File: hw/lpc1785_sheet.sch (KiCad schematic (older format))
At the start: 26 parts, among them J2 ARM_JTAG_SWD_HEADER_10_PINSMD, J3 HEADER_USART_2_SMD, U4 LPC1785FBD208_551QFP50, X1 XTAL_7A-20.000MAAJ-T

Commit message: PCB was too big for itead, reduced size and ordered one
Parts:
- J3: footprint usevolt:usevolt-HEADER_4_2_SMD -> usevolt:HEADER_4_2_SMD
- U4: footprint usevolt:usevolt-QFP208 -> usevolt:QFP208
- X1: footprint usevolt:usevolt-XTAL_7A-20.000MAJ -> usevolt:XTAL_7A-20.000MAJ
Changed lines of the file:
@@
 F 0 "U4" H 7150 7354 45  0000 C CNN
 F 1 "LPC1785FBD208_551QFP50" H 7150 7270 45  0000 C CNN
-F 2 "usevolt:usevolt-QFP208" H 6730 5550 20  0001 C CNN
+F 2 "usevolt:QFP208" H 6730 5550 20  0001 C CNN
 F 3 "http://www.nxp.com/documents/data_sheet/LPC178X_7X.pdf" H 6871 7282 60  0001 C CNN
 F 4 "568-7573-ND" H 7271 7682 60  0001 C CNN "1st Source Part Number"
@@
 F 0 "U4" H 14150 6804 45  0000 C CNN
 F 1 "LPC1785FBD208_551QFP50" H 14150 6720 45  0000 C CNN
-F 2 "usevolt:usevolt-QFP208" H 13030 5200 20  0001 C CNN
+F 2 "usevolt:QFP208" H 13030 5200 20  0001 C CNN
 F 3 "http://www.nxp.com/documents/data_sheet/LPC178X_7X.pdf" H 13171 6932 60  0001 C CNN
 F 4 "568-7573-ND" H 13571 7332 60  0001 C CNN "1st Source Part Number"
@@
 F 0 "U4" H 7050 12154 45  0000 C CNN
 F 1 "LPC1785FBD208_551QFP50" H 7050 12070 45  0000 C CNN
-F 2 "usevolt:usevolt-QFP208" H 5980 10650 20  0001 C CNN
+F 2 "usevolt:QFP208" H 5980 10650 20  0001 C CNN
 F 3 "http://www.nxp.com/documents/data_sheet/LPC178X_7X.pdf" H 6121 12382 60  0001 C CNN
 F 4 "568-7573-ND" H 6521 12782 60  0001 C CNN "1st Source Part Number"
@@
 F 0 "U4" H 13800 12554 45  0000 C CNN
 F 1 "LPC1785FBD208_551QFP50" H 13800 12470 45  0000 C CNN
-F 2 "usevolt:usevolt-QFP208" H 12830 10750 20  0001 C CNN
+F 2 "usevolt:QFP208" H 12830 10750 20  0001 C CNN
 F 3 "http://www.nxp.com/documents/data_sheet/LPC178X_7X.pdf" H 12971 12482 60  0001 C CNN
 F 4 "568-7573-ND" H 13371 12882 60  0001 C CNN "1st Source Part Number"
@@
 F 0 "X1" V 11508 9498 45  0000 L CNN
 F 1 "XTAL_7A-20.000MAAJ-T" V 11592 9498 45  0000 L CNN
-F 2 "usevolt:usevolt-XTAL_7A-20.000MAJ" H 11630 9550 20  0001 C CNN
+F 2 "usevolt:XTAL_7A-20.000MAJ" H 11630 9550 20  0001 C CNN
 F 3 "http://www.farnell.com/datasheets/1041607.pdf?_ga=1.225290842.1948984246.1460023966" H 11620 9420 60  0001 C CNN
 F 4 "1841950" H 12020 9820 60  0001 C CNN "1st Source Part Number"
@@
 F 0 "J3" H 19077 10292 45  0000 L CNN
 F 1 "HEADER_USART_2_SMD" H 19077 10208 45  0000 L CNN
-F 2 "usevolt:usevolt-HEADER_4_2_SMD" H 18680 10550 20  0001 C CNN
+F 2 "usevolt:HEADER_4_2_SMD" H 18680 10550 20  0001 C CNN
 F 3 "" H 18650 10400 60  0000 C CNN
 	1    18650 10400
@@
 $Bitmap
 Pos 22650 15250
-Scale 1,000000
+Scale 1.000000
 Data
 89 50 4E 47 0D 0A 1A 0A 00 00 00 0D 49 48 44 52 00 00 00 7B 00 00 00 49 08 02 00 00 00 92 17 CE

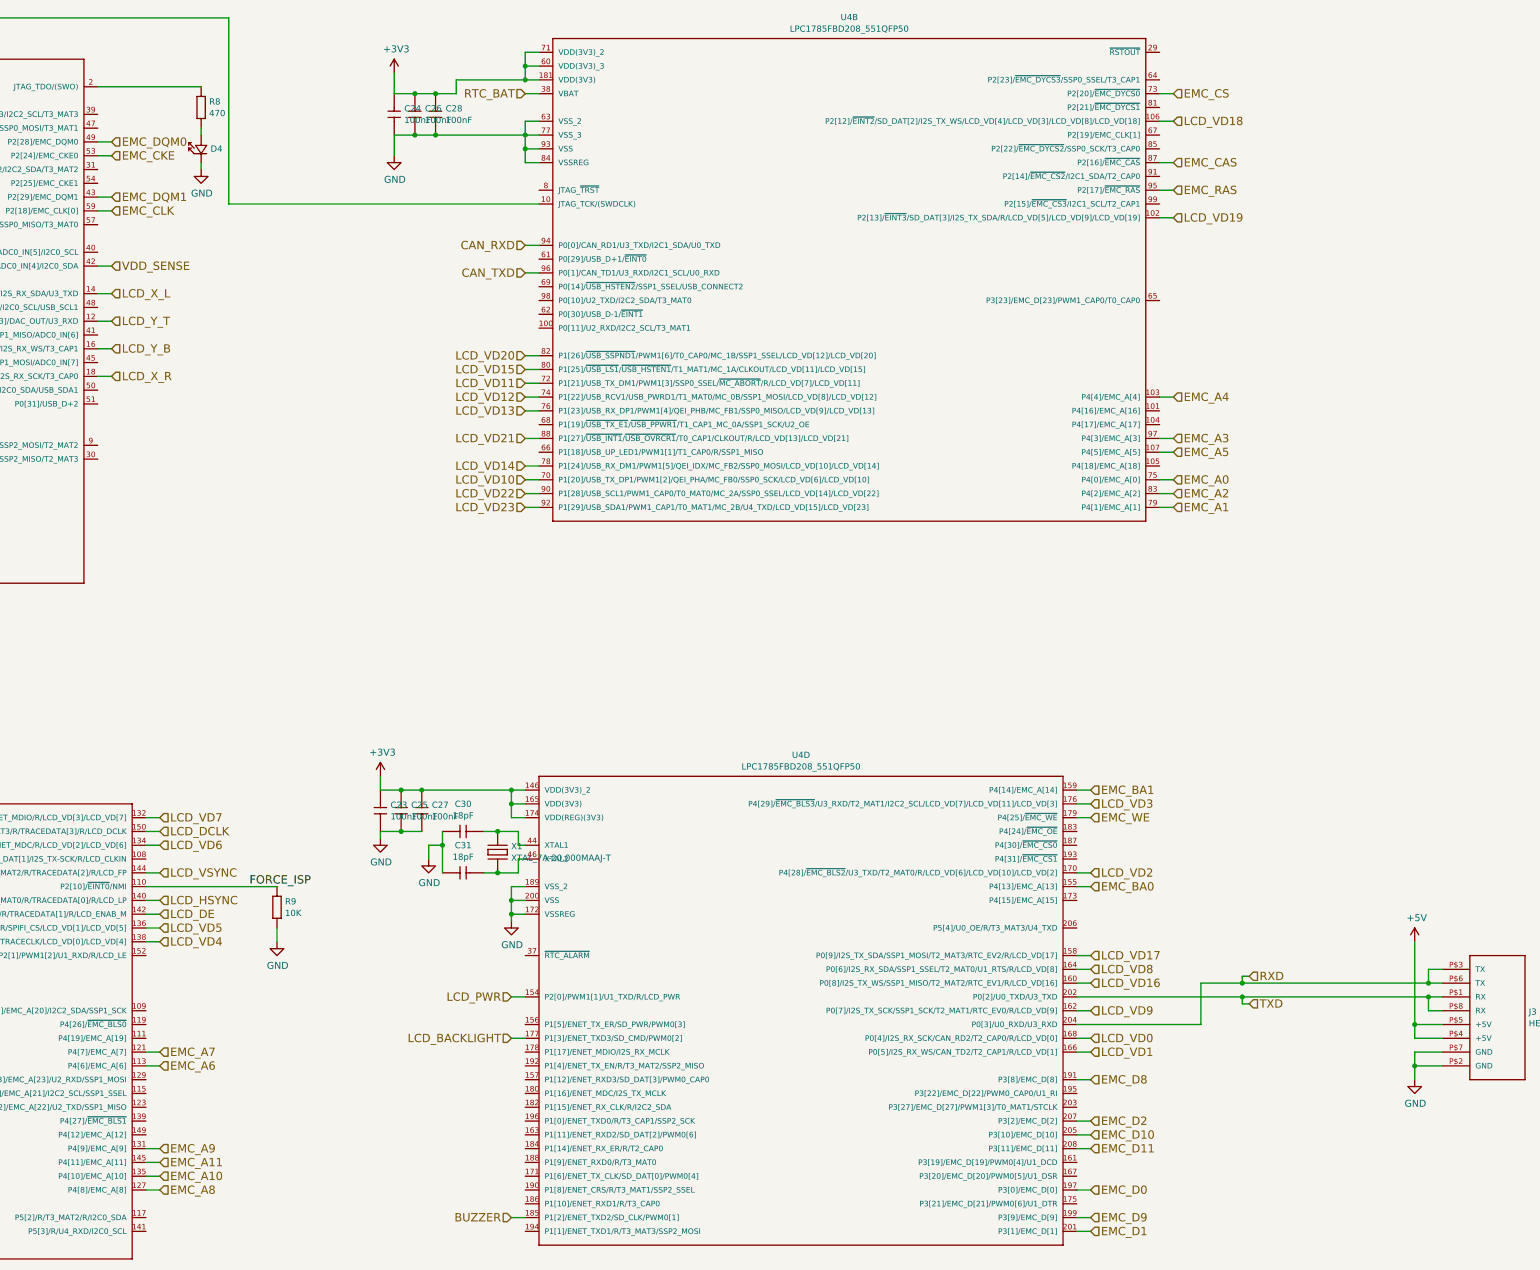
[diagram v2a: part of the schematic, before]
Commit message: HW revision 3 ordered from itead
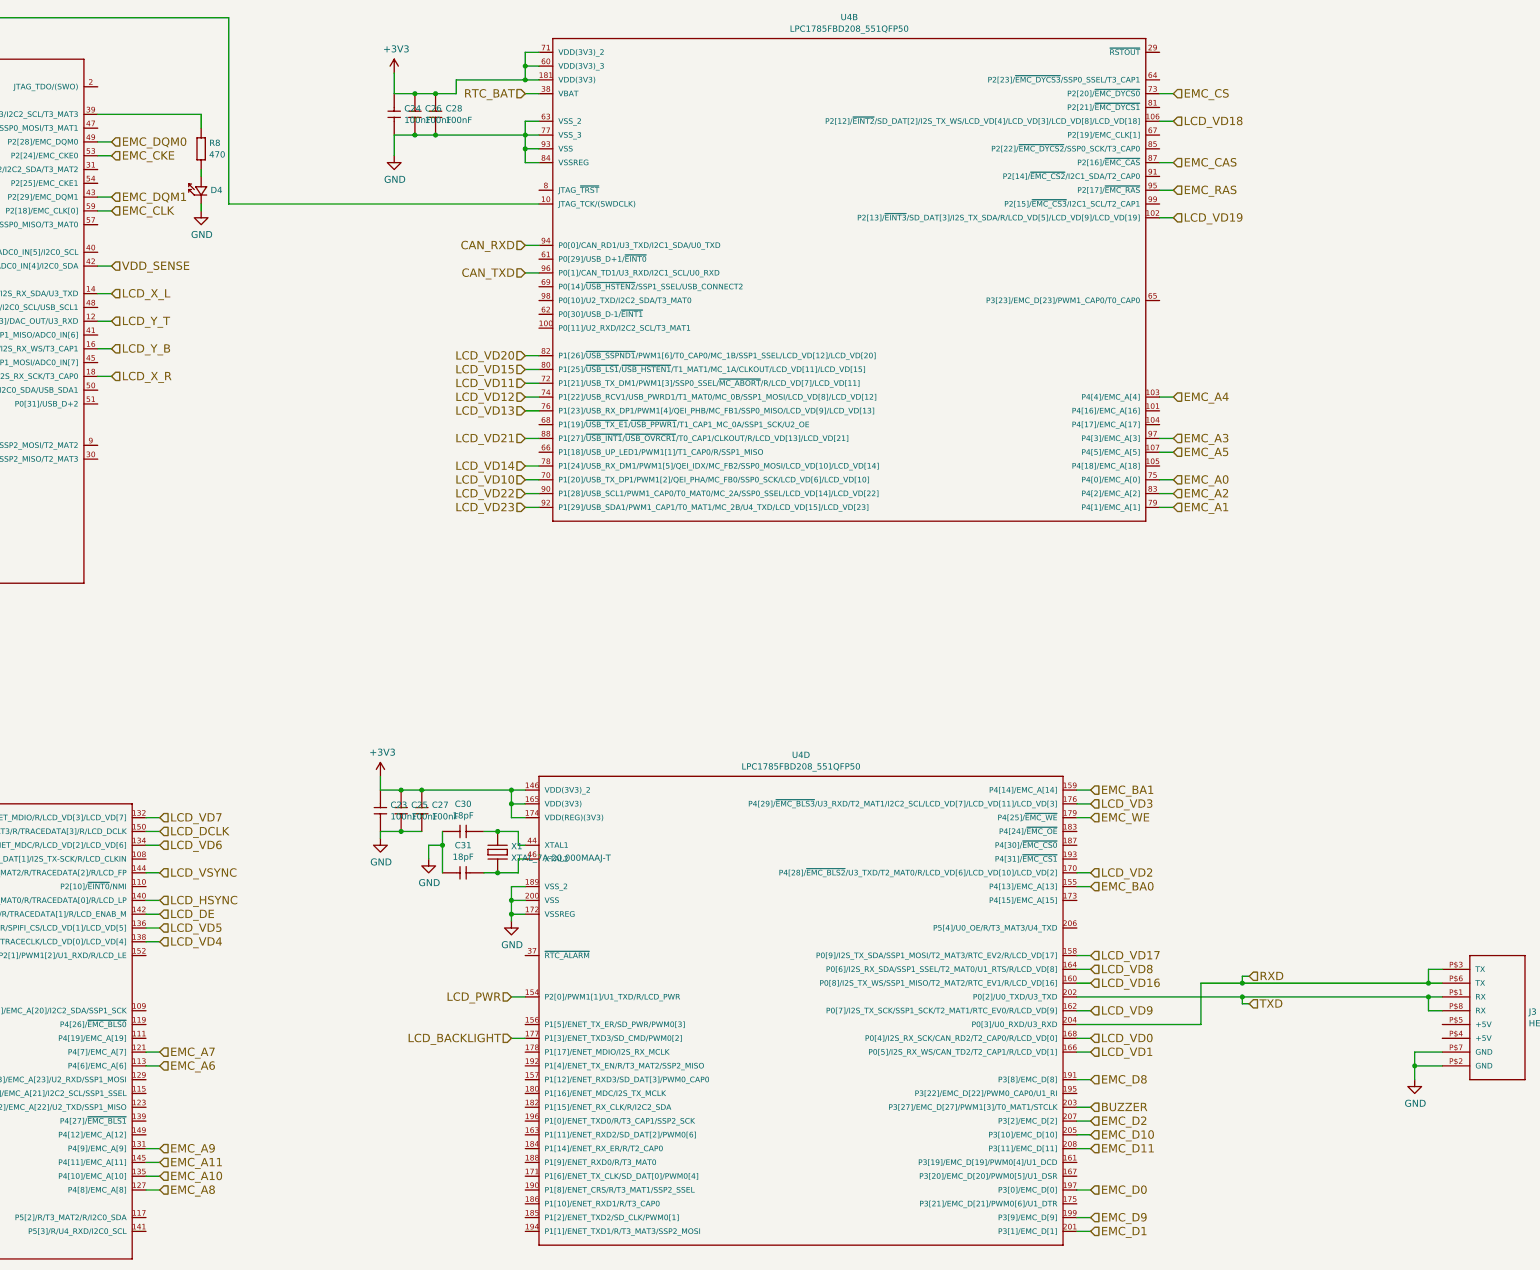
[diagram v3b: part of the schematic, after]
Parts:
- removed R9: 10K, multicomp:Multicomp-RESC1608X60N, symbol 10K
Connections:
- net BUZZER: now also U4.203 (P3[27]/EMC_D[27]/PWM1[3]/T0_MAT1/STCLK); no longer U4.185 (P1[2]/ENET_TXD2/SD_CLK/PWM0[1])
- net at U4.2 (JTAG_TDO/(SWO)): no longer R8.2 (R2)
- net at U4.39 (P2[31]/EMC_DQM3/I2C2_SCL/T3_MAT3): now also R8.2 (R2)
- net +5V: no longer names the net of J3.P$4 (+5V)
- net +5V: no longer J3.P$5 (+5V)
- net FORCE_ISP: no longer names the net of U4.110 (P2[10]/~EINT0~/NMI)
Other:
- moved on the sheet: D4, R8
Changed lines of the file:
@@
 L 470 R8
 U 1 1 57B5BC06
-P 9450 3900
-F 0 "R8" V 9458 3958 45  0000 L CNN
-F 1 "470" V 9542 3958 45  0000 L CNN
-F 2 "multicomp:Multicomp-RESC1608X60N" H 9480 4050 20  0001 C CNN
-F 3 "" H 9419 3939 60  0001 C CNN
-F 4 "9331239" H 9819 4339 60  0001 C CNN "1st Source Part Number"
-F 5 "Farnell" H 9719 4239 60  0001 C CNN "1st Source"
-F 6 "MC0063W06031470R" H 9619 4139 60  0001 C CNN "Manufacturer Part Number"
-F 7 "MULTICOMP" H 9519 4039 60  0001 C CNN "Manufacturer"
-	1    9450 3900
-	0    1    1    0
-$EndComp
-Wire Wire Line
-	9450 4150 9450 4100
-Wire Wire Line
-	9450 3800 8700 3800
+P 9450 4200
+F 0 "R8" V 9458 4258 45  0000 L CNN
+F 1 "470" V 9542 4258 45  0000 L CNN
+F 2 "multicomp:Multicomp-RESC1608X60N" H 9480 4350 20  0001 C CNN
+F 3 "" H 9419 4239 60  0001 C CNN
+F 4 "9331239" H 9819 4639 60  0001 C CNN "1st Source Part Number"
+F 5 "Farnell" H 9719 4539 60  0001 C CNN "1st Source"
+F 6 "MC0063W06031470R" H 9619 4439 60  0001 C CNN "Manufacturer Part Number"
+F 7 "MULTICOMP" H 9519 4339 60  0001 C CNN "Manufacturer"
+	1    9450 4200
+	0    1    1    0
+$EndComp
+Wire Wire Line
+	9450 4450 9450 4400
 $Comp
 L WL-SMCW-150060BS75000-B D4
 U 1 1 57B5C226
-P 9450 4250
-F 0 "D4" V 9450 4182 45  0000 R CNN
-F 1 "WL-SMCW-150060BS75000-B" H 9650 4350 45  0001 L BNN
-F 2 "wurth_LEDS:Wuerth_Elektronik_LEDs_rev15b-0603" H 9480 4400 20  0001 C CNN
-F 3 "http://www.farnell.com/datasheets/1911343.pdf?_ga=1.259491274.1948984246.1460023966" H 9250 4450 60  0001 C CNN
-F 4 "150060BS75000" H 9659 4453 60  0001 C CNN "Manufacturer Part Number"
-F 5 "2322069" H 9859 4653 60  0001 C CNN "1st Source Part Number"
-F 6 "Farnell" H 9759 4553 60  0001 C CNN "1st Source"
-F 7 "WURTH ELEKTRONIK" H 9559 4353 60  0001 C CNN "Manufacturer"
-	1    9450 4250
+P 9450 4550
+F 0 "D4" V 9450 4482 45  0000 R CNN
+F 1 "WL-SMCW-150060BS75000-B" H 9650 4650 45  0001 L BNN
+F 2 "wurth_LEDS:Wuerth_Elektronik_LEDs_rev15b-0603" H 9480 4700 20  0001 C CNN
+F 3 "http://www.farnell.com/datasheets/1911343.pdf?_ga=1.259491274.1948984246.1460023966" H 9250 4750 60  0001 C CNN
+F 4 "150060BS75000" H 9659 4753 60  0001 C CNN "Manufacturer Part Number"
+F 5 "2322069" H 9859 4953 60  0001 C CNN "1st Source Part Number"
+F 6 "Farnell" H 9759 4853 60  0001 C CNN "1st Source"
+F 7 "WURTH ELEKTRONIK" H 9559 4653 60  0001 C CNN "Manufacturer"
+	1    9450 4550
 	0    -1   -1   0
 $EndComp
@@
 L GND #PWR032
 U 1 1 57B5C2C2
-P 9450 4400
-F 0 "#PWR032" H 9450 4150 50  0001 C CNN
-F 1 "GND" H 9455 4227 50  0000 C CNN
-F 2 "" H 9450 4400 50  0000 C CNN
-F 3 "" H 9450 4400 50  0000 C CNN
-	1    9450 4400
-	1    0    0    -1
-$EndComp
-Wire Wire Line
-	9450 4400 9450 4350
+P 9450 4700
+F 0 "#PWR032" H 9450 4450 50  0001 C CNN
+F 1 "GND" H 9455 4527 50  0000 C CNN
+F 2 "" H 9450 4700 50  0000 C CNN
+F 3 "" H 9450 4700 50  0000 C CNN
+	1    9450 4700
+	1    0    0    -1
+$EndComp
+Wire Wire Line
+	9450 4700 9450 4650
 Text HLabel 8800 4200 2    60   Input ~ 0
 EMC_DQM0
@@
 Wire Wire Line
 	9150 9800 9050 9800
-$Comp
-L 10K R9
-U 1 1 57B6C633
-P 10000 9700
-F 0 "R9" V 10008 9758 45  0000 L CNN
-F 1 "10K" V 10092 9758 45  0000 L CNN
-F 2 "multicomp:Multicomp-RESC1608X60N" H 10030 9850 20  0001 C CNN
-F 3 "http://www.farnell.com/datasheets/1788326.pdf?_ga=1.214208087.1948984246.1460023966" H 9969 9739 60  0001 C CNN
-F 4 "9330399" H 10369 10139 60  0001 C CNN "1st Source Part Number"
-F 5 "Farnell" H 10269 10039 60  0001 C CNN "1st Source"
-F 6 "MC0063W0603110K" H 10169 9939 60  0001 C CNN "Manufacturer Part Number"
-F 7 "MULTICOMP" H 10069 9839 60  0001 C CNN "Manufacturer"
-	1    10000 9700
-	0    1    1    0
-$EndComp
-Wire Wire Line
-	10000 9600 9050 9600
-$Comp
-L GND #PWR033
-U 1 1 57B6C7FA
-P 10000 10000
-F 0 "#PWR033" H 10000 9750 50  0001 C CNN
-F 1 "GND" H 10005 9827 50  0000 C CNN
-F 2 "" H 10000 10000 50  0000 C CNN
-F 3 "" H 10000 10000 50  0000 C CNN
-	1    10000 10000
-	1    0    0    -1
-$EndComp
-Wire Wire Line
-	10000 9900 10000 10000
-Text Label 9800 9600 0    60   ~ 0
-FORCE_ISP
 Text HLabel 9150 10800 2    60   Input ~ 0
 EMC_A7
@@
 Connection ~ 11700 9000
 $Comp
-L GND #PWR034
+L GND #PWR033
 U 1 1 57B6EDB0
 P 10750 9250
-F 0 "#PWR034" H 10750 9000 50  0001 C CNN
+F 0 "#PWR033" H 10750 9000 50  0001 C CNN
 F 1 "GND" H 10755 9077 50  0000 C CNN
 F 2 "" H 10750 9250 50  0000 C CNN
@@
 	11200 9200 11200 9500
 $Comp
-L GND #PWR035
+L GND #PWR034
 U 1 1 57B6F87A
 P 11100 9400
-F 0 "#PWR035" H 11100 9150 50  0001 C CNN
+F 0 "#PWR034" H 11100 9150 50  0001 C CNN
 F 1 "GND" H 11105 9227 50  0000 C CNN
 F 2 "" H 11100 9400 50  0000 C CNN
@@
 Connection ~ 11700 9700
 $Comp
-L GND #PWR036
+L GND #PWR035
 U 1 1 57B7073F
 P 11700 9850
-F 0 "#PWR036" H 11700 9600 50  0001 C CNN
+F 0 "#PWR035" H 11700 9600 50  0001 C CNN
 F 1 "GND" H 11705 9677 50  0000 C CNN
 F 2 "" H 11700 9850 50  0000 C CNN
@@
 Wire Wire Line
 	11700 10700 11800 10700
-Text HLabel 11700 12000 0    60   Input ~ 0
+Text HLabel 15900 11200 2    60   Input ~ 0
 BUZZER
-Wire Wire Line
-	11700 12000 11800 12000
 Text HLabel 15900 12100 2    60   Input ~ 0
 EMC_D1
@@
 Connection ~ 18350 10300
 $Comp
-L +5V #PWR037
-U 1 1 57B76E94
-P 18250 10000
-F 0 "#PWR037" H 18250 9850 50  0001 C CNN
-F 1 "+5V" H 18265 10173 50  0000 C CNN
-F 2 "" H 18250 10000 50  0000 C CNN
-F 3 "" H 18250 10000 50  0000 C CNN
-	1    18250 10000
-	1    0    0    -1
-$EndComp
-Wire Wire Line
-	18250 10000 18250 10700
-Wire Wire Line
-	18250 10600 18450 10600
-Wire Wire Line
-	18250 10700 18450 10700
-Connection ~ 18250 10600
-$Comp
-L GND #PWR038
+L GND #PWR036
 U 1 1 57B77105
 P 18250 11000
-F 0 "#PWR038" H 18250 10750 50  0001 C CNN
+F 0 "#PWR036" H 18250 10750 50  0001 C CNN
 F 1 "GND" H 18255 10827 50  0000 C CNN
 F 2 "" H 18250 11000 50  0000 C CNN
@@
 SPI_RESET
 $Comp
-L +3V3 #PWR039
+L +3V3 #PWR037
 U 1 1 57BCA081
 P 10750 8800
-F 0 "#PWR039" H 10750 8650 50  0001 C CNN
+F 0 "#PWR037" H 10750 8650 50  0001 C CNN
 F 1 "+3V3" H 10765 8973 50  0000 C CNN
 F 2 "" H 10750 8800 50  0000 C CNN
@@
 	10750 8800 10750 8900
 $Comp
-L +3V3 #PWR040
+L +3V3 #PWR038
 U 1 1 57BCA489
 P 4400 9250
-F 0 "#PWR040" H 4400 9100 50  0001 C CNN
+F 0 "#PWR038" H 4400 9100 50  0001 C CNN
 F 1 "+3V3" H 4415 9423 50  0000 C CNN
 F 2 "" H 4400 9250 50  0000 C CNN
@@
 	4400 9250 4400 9400
 $Comp
-L +3V3 #PWR041
+L +3V3 #PWR039
 U 1 1 57BCB2A0
 P 10850 3700
-F 0 "#PWR041" H 10850 3550 50  0001 C CNN
+F 0 "#PWR039" H 10850 3550 50  0001 C CNN
 F 1 "+3V3" H 10865 3873 50  0000 C CNN
 F 2 "" H 10850 3700 50  0000 C CNN
@@
 	10850 3700 10850 3850
 $Comp
-L GND #PWR042
+L GND #PWR040
 U 1 1 57BCB9E7
 P 10850 4300
-F 0 "#PWR042" H 10850 4050 50  0001 C CNN
+F 0 "#PWR040" H 10850 4050 50  0001 C CNN
 F 1 "GND" H 10855 4127 50  0000 C CNN
 F 2 "" H 10850 4300 50  0000 C CNN
@@
 	10850 4300 10850 4150
 $Comp
-L GND #PWR043
+L GND #PWR041
 U 1 1 57BCC515
 P 4400 9850
-F 0 "#PWR043" H 4400 9600 50  0001 C CNN
+F 0 "#PWR041" H 4400 9600 50  0001 C CNN
 F 1 "GND" H 4405 9677 50  0000 C CNN
 F 2 "" H 4400 9850 50  0000 C CNN
@@
 Wire Wire Line
 	4700 4300 5150 4300
+Wire Wire Line
+	15900 11200 15800 11200
+Wire Wire Line
+	9450 4100 9450 4000
+Wire Wire Line
+	9450 4000 8700 4000
 $EndSCHEMATC
